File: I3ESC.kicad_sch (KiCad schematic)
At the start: 54 parts, among them J10 VIN_BARREL, J13 Conn_SWD, J5 Encoder1, J7 VIN_TERMINAL, J8 Encoder2, SW2 boot-red, SW3 user1-white, U1 SY8113BADC, U3 SPX3819M5-L-3-3, U4 STM32G474RETx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

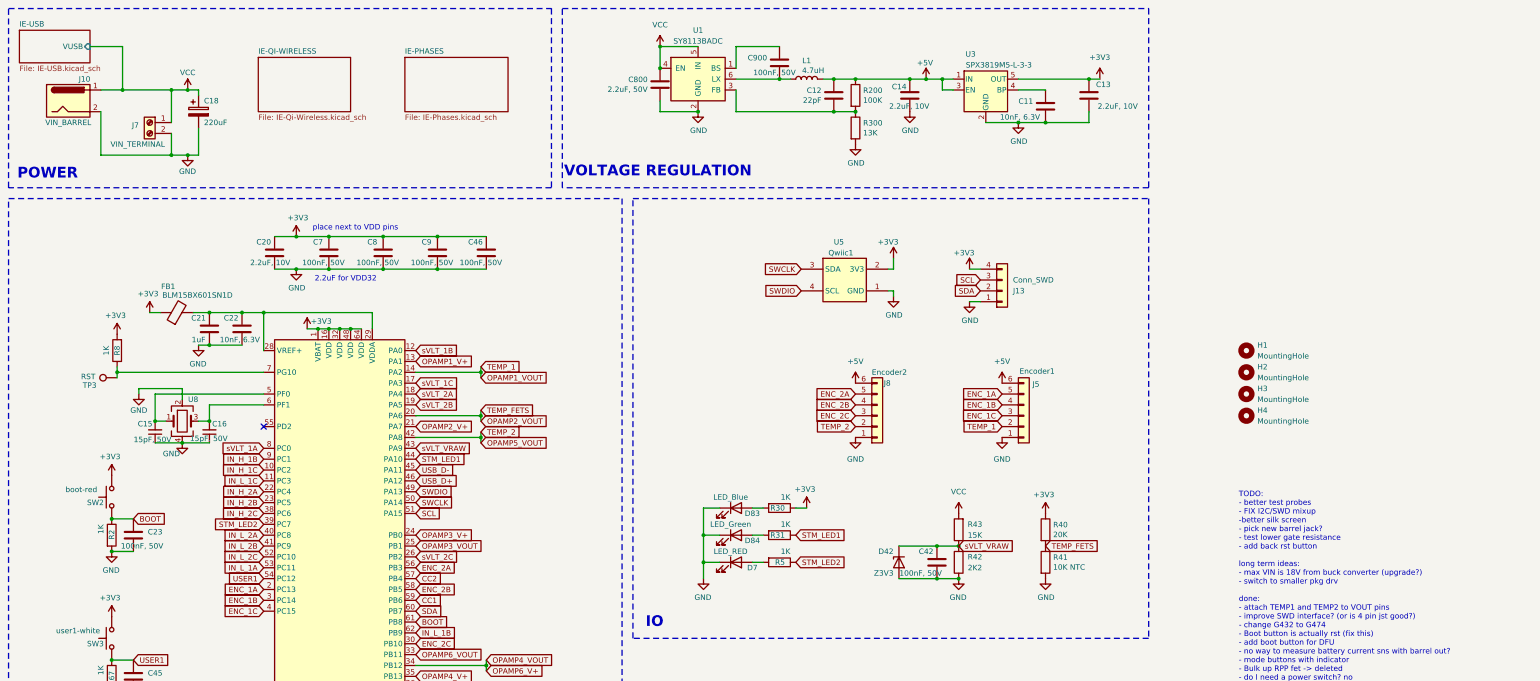
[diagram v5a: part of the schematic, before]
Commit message: Refactor net naming and update component values
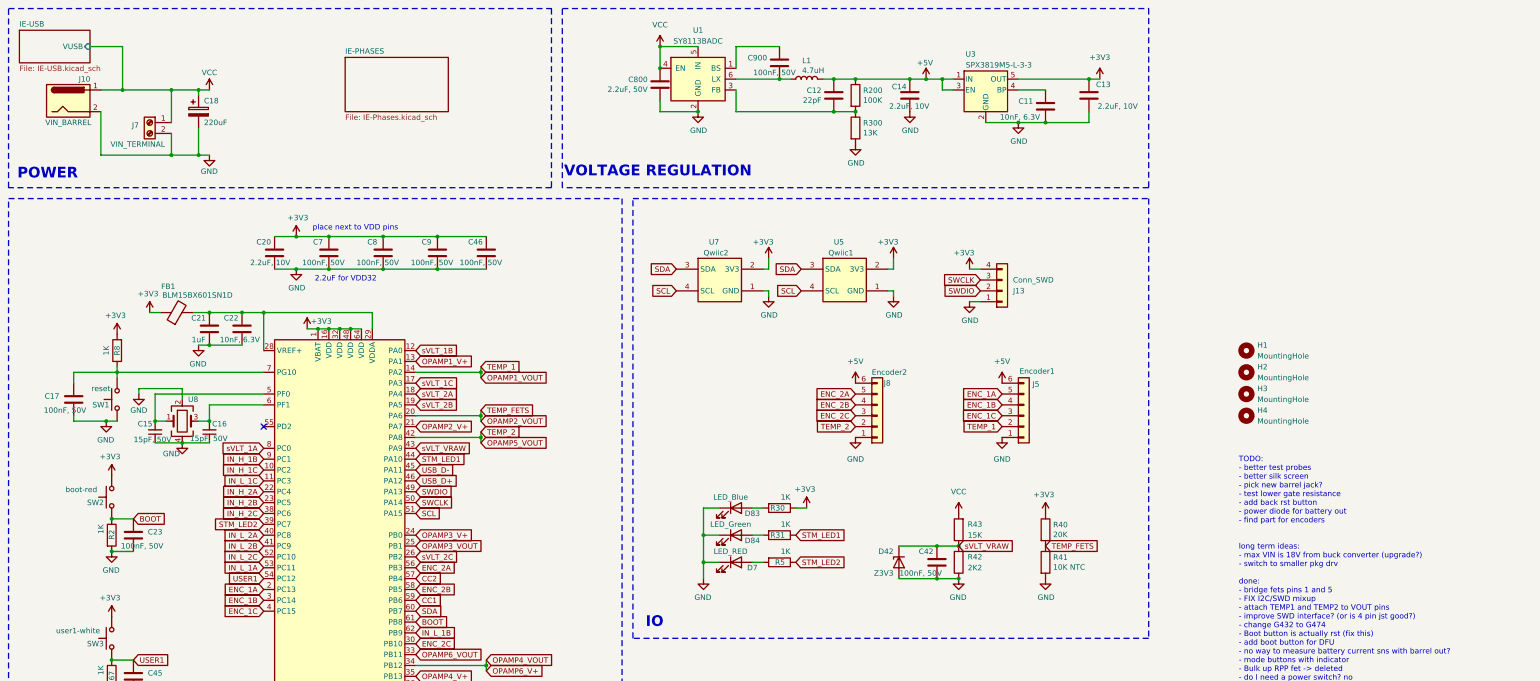
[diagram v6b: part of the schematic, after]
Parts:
- removed TP3: RST, AlfredoFootprints:GE_TestPoint_Loop, symbol Connector:TestPoint
- added C17: 100nF, 50V, Capacitor_SMD:C_0402_1005Metric, symbol Device:C
- added SW1: reset, AlfredoFootprints:Button_SKRKAEE020, symbol Switch:SW_Push
- added U7: Qwiic2, Connector_JST:JST_SH_BM04B-SRSS-TB_1x04-1MP_P1.00mm_Vertical, symbol AlfredoSymbols:QwiicConnector
- J5, J8: LCSC (none) -> C131342
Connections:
- net +3V3: now also U7.2 (3V3)
- net GND: now also C17.2, SW1.2, U7.1 (GND)
- net SCL: now also U5.4 (SCL), U7.4 (SCL); no longer J13.3 (Pin_3)
- net SDA: now also U5.3 (SDA), U7.3 (SDA); no longer J13.2 (Pin_2)
- net SWCLK: now also J13.3 (Pin_3); no longer U5.3 (SDA)
- net SWDIO: now also J13.2 (Pin_2); no longer U5.4 (SCL)
- net at R8.1, U4.7 (PG10): now also C17.1, SW1.1
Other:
- removed sheet IE-QI-WIRELESS
- note added: "TODO: - better test probes - better silk screen - pick new barrel jack? - test lower gate resistance - add back rst button - power diode for battery out - find part for encoders long term ideas: - max VIN is 18V from buck converter (upgrade?) - switch to smaller pkg drv done: - bridge fets pins 1 and 5 - FIX I2C/SWD mixup - attach TEMP1 and TEMP2 to VOUT pins - improve SWD interface? (or is 4 pin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"
- note removed: "TODO: - better test probes - FIX I2C/SWD mixup -better silk screen - pick new barrel jack? - test lower gate resistance - add back rst button long term ideas: - max VIN is 18V from buck converter (upgrade?) - switch to smaller pkg drv done: - attach TEMP1 and TEMP2 to VOUT pins - improve SWD interface? (or is 4 pin jst good?) - change G432 to G474 - Boot button is actually rst (fix this) - add bo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"

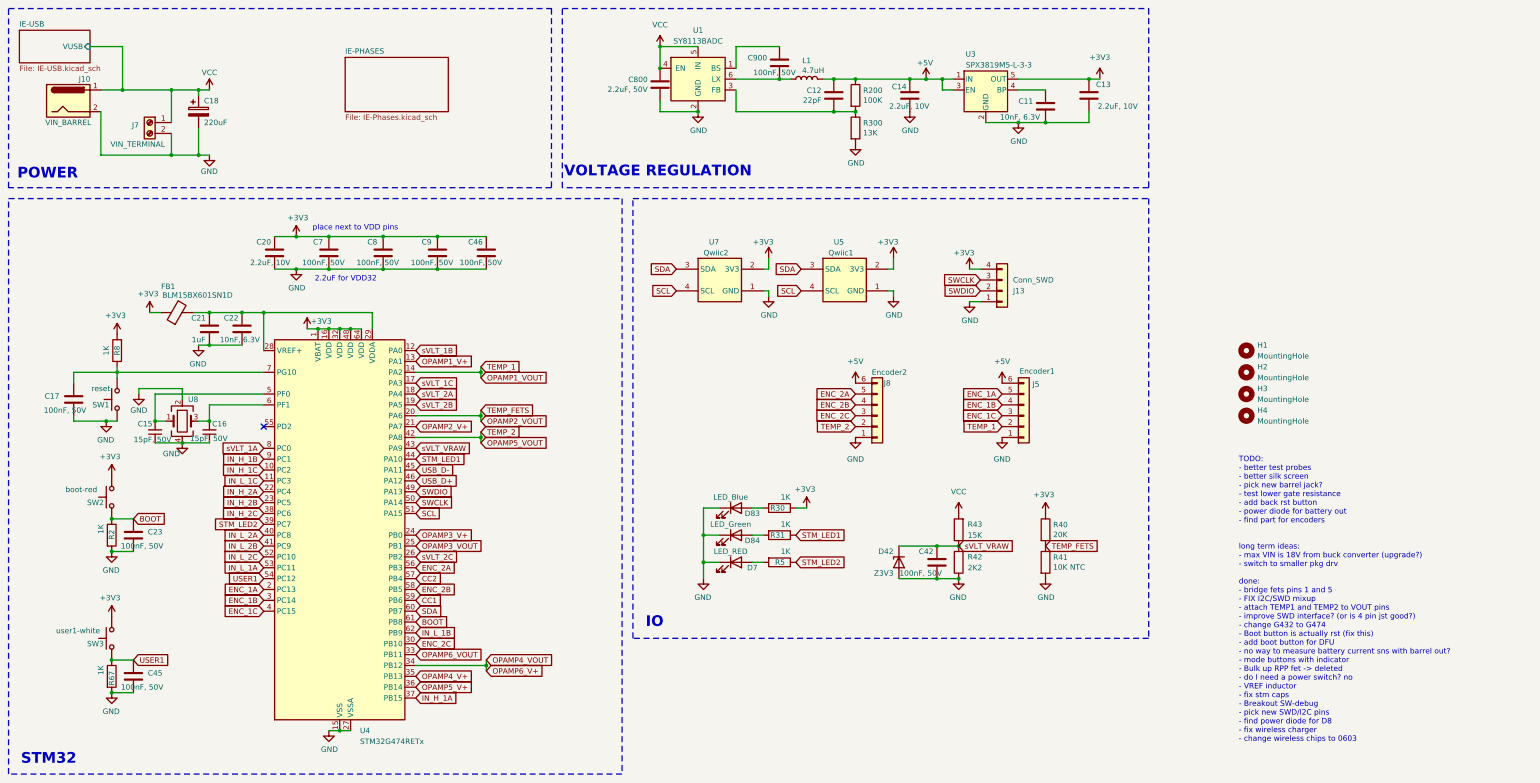
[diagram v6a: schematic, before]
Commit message: Add decoupling capacitor to PG10 and update footprints
Added C17 (100nF, 50V) capacitor to PG10 for improved decoupling. Updated several footprint and property fields, fixed layer and sheetname attributes, and made minor net and pad stack changes for consistency with KiCAD 9.0. Updated LCSC part number for JST SH connector.
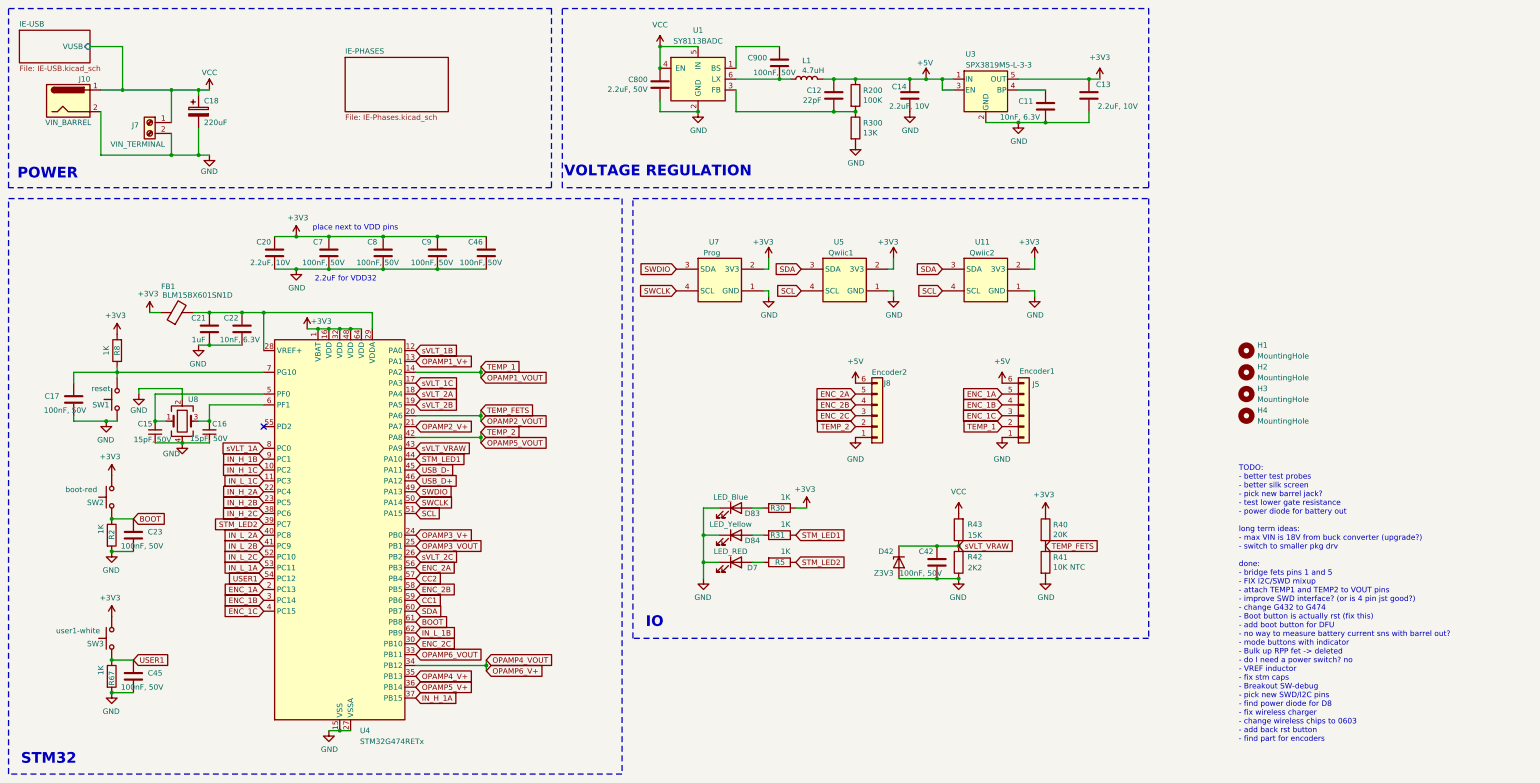
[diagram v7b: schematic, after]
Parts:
- removed J13: Conn_SWD, Connector_PinHeader_2.54mm:PinHeader_1x04_P2.54mm_Vertical, symbol Connector_Generic:Conn_01x04
- added U11: Qwiic2, Connector_JST:JST_SH_BM04B-SRSS-TB_1x04-1MP_P1.00mm_Vertical, symbol AlfredoSymbols:QwiicConnector
- D42: LCSC C2891760 -> C131795
- D84: value LED_Green -> LED_Yellow; LCSC (none) -> C2290
- J5: LCSC C131342 -> C131342
- J7: LCSC C557646 -> C8404
- L1: LCSC C98354 -> C86070
- U5: LCSC C160390 -> C18077917
- U7: value Qwiic2 -> Prog; LCSC C160390 -> C18077917
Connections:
- net +3V3: now also U11.2 (3V3)
- net GND: now also U11.1 (GND)
- net SCL: now also U11.4 (SCL); no longer U7.4 (SCL)
- net SDA: now also U11.3 (SDA); no longer U7.3 (SDA)
- net SWCLK: now also U7.4 (SCL)
- net SWDIO: now also U7.3 (SDA)
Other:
- note added: "TODO: - better test probes - better silk screen - pick new barrel jack? - test lower gate resistance - power diode for battery out long term ideas: - max VIN is 18V from buck converter (upgrade?) - switch to smaller pkg drv done: - bridge fets pins 1 and 5 - FIX I2C/SWD mixup - attach TEMP1 and TEMP2 to VOUT pins - improve SWD interface? (or is 4 pin jst good?) - change G432 to G474 - Boot button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"
- note removed: "TODO: - better test probes - better silk screen - pick new barrel jack? - test lower gate resistance - add back rst button - power diode for battery out - find part for encoders long term ideas: - max VIN is 18V from buck converter (upgrade?) - switch to smaller pkg drv done: - bridge fets pins 1 and 5 - FIX I2C/SWD mixup - attach TEMP1 and TEMP2 to VOUT pins - improve SWD interface? (or is 4 pin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"
